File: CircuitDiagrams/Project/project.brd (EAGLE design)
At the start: 100 x 70 mm, 123 parts, among them IC1 UC3C, IC2 PCA9542A, IC3 MT48LC4M16A2TSOP54, IC4 TB6593FNGSSOP20, IC5 TB6593FNGSSOP20, J2 1BY2THROUGHHOLE, J3 1BY2THROUGHHOLE, J4 1BY2THROUGHHOLE, J5 8PIN1.27MM2X4TH, J6 4PIN1.27MM2X2TH, J7 1BY2THROUGHHOLE, J8 10PIN1.27MM2X5TH, Q1 OV7670, Q2 OV7670, Q3 VREGSOT-223, Q4 TCRT1010TH, Q5 TCRT1010TH, Q6 CSM-7X-DU, X2 MICROSDSMD

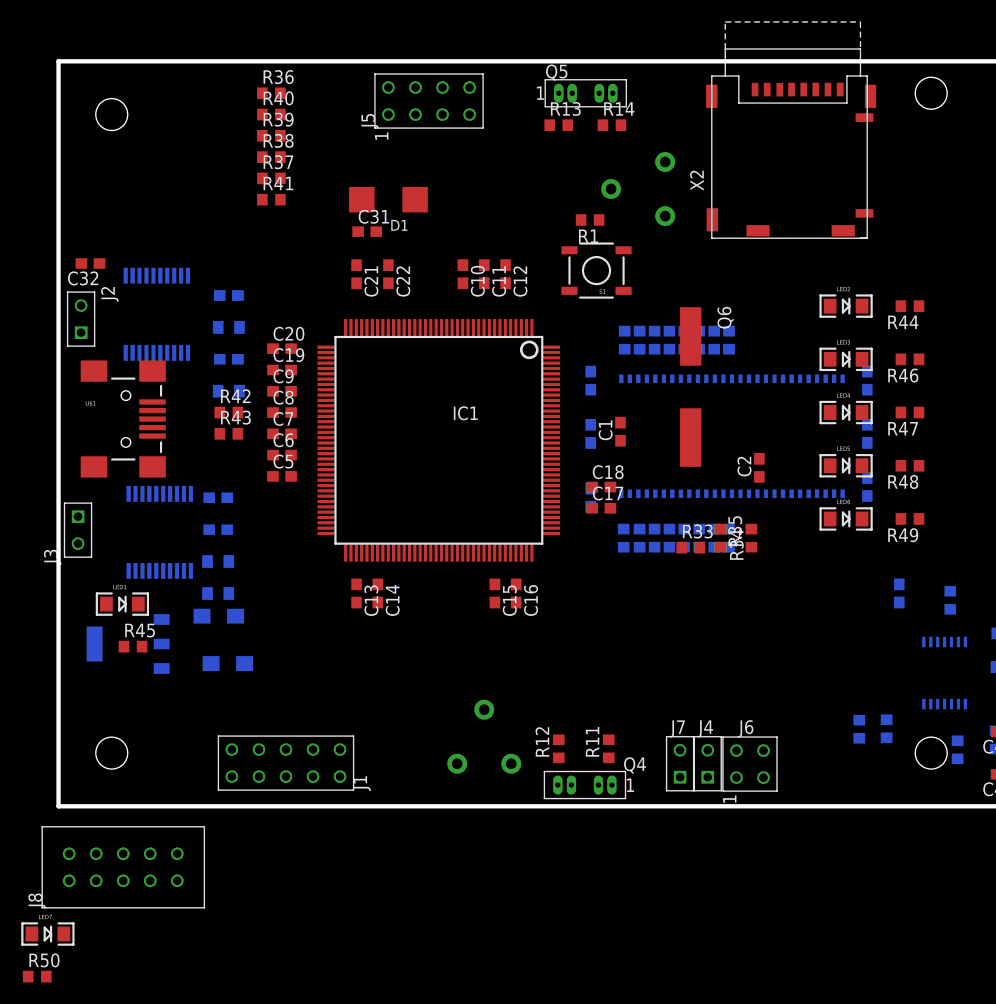
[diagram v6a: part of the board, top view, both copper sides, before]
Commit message: Changed the JTAG Package. Added Headers for all unused pins.
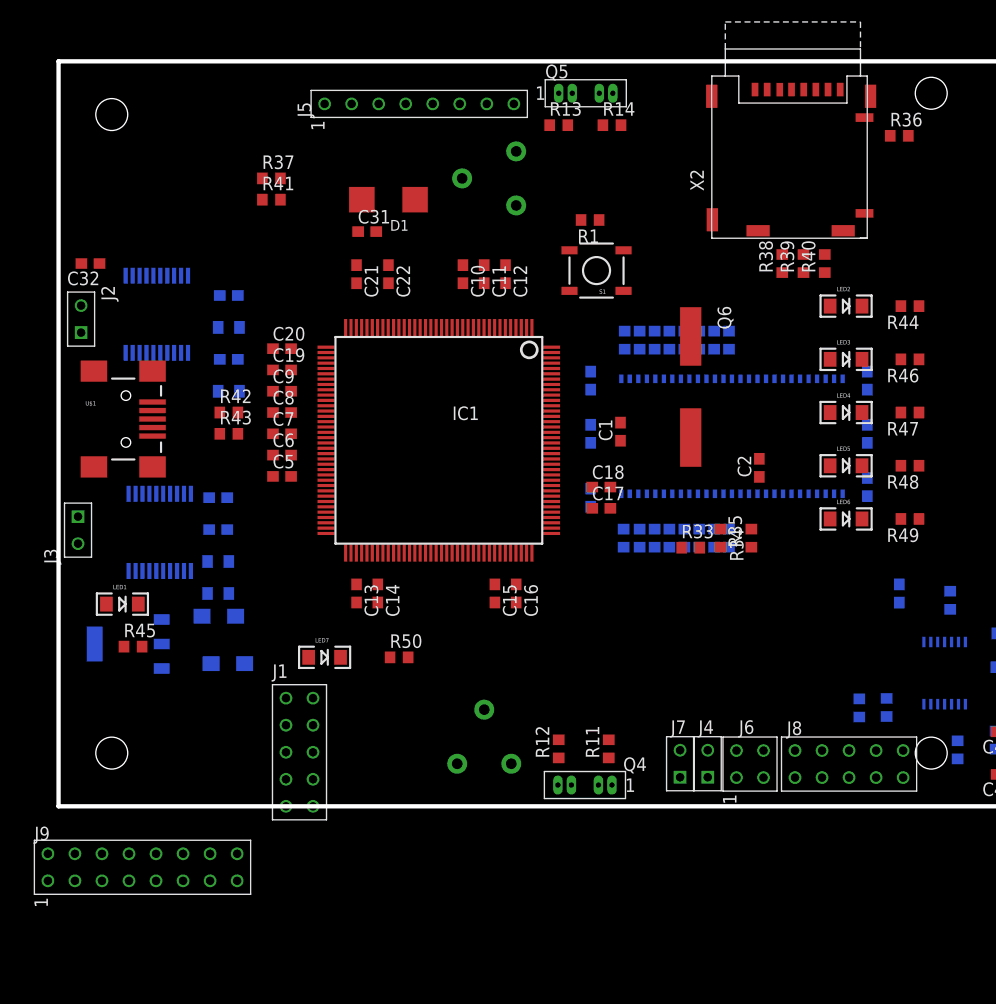
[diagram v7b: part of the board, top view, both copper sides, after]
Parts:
- added J9: 16PIN2.54MM2X8TH, Headers:2.54MM2X8TH
- J1: value (none) -> JTAG2.54MM2X5TH; device Headers:2BY5 -> Headers:2.54MM2X5TH
- J5: value 8PIN1.27MM2X4TH -> 8PIN2.54MM1X8TH; device Headers:1.27MM2X4TH -> Headers:2.54MM1X8TH
- J6: value 4PIN1.27MM2X2TH -> 4PIN2.54MM2X2TH; device Headers:1.27MM2X2TH -> Headers:2.54MM2X2TH
- J8: value 10PIN1.27MM2X5TH -> 10PIN2.54MM2X5TH; device Headers:1.27MM2X5TH -> Headers:2.54MM2X5TH
- moved J8 68.9 mm to (69.2, 2.70)
- moved R36 59.1 mm to (79.0, 63.0)
- moved R40 53.9 mm to (72.0, 51.0), turned to 90 degrees
- moved R39 51.4 mm to (70.0, 51.0), turned to 90 degrees
- moved R38 49.0 mm to (68.0, 51.0), turned to 90 degrees
- moved R50 45.3 mm to (32.0, 14.0)
- moved LED7 36.8 mm to (25.0, 14.0)
- moved R16 14.0 mm to (43.0, 59.0)
- moved J1 6.10 mm to (21.4, 10.2)
- moved J5 6.08 mm to (25.0, 66.0)
- moved R3 2.00 mm to (75.2, 9.24)
- moved R2 2.00 mm to (77.8, 9.29)
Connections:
- net PA10: now also J8.7; no longer J8.2
- net PA12: now also J8.8; no longer J8.3
- net PA13: now also J8.9; no longer J8.4
- net PA14: now also J8.10; no longer J8.5
- net PA5: now also J8.6; no longer J8.1
- net PC0: now also J9.16; no longer J8.10
- net PC1: now also J9.15; no longer J8.9
- net PC10: now also J9.11
- net PC11: now also J9.10
- net PC12: now also J9.9
- net PC13: now also J9.8; no longer J8.7
- net PC6: now also J9.14; no longer J8.8
- net PC7: now also J9.13
- net PC9: now also J9.12
- net PD16: now also J8.2
- net PD18: now also J8.3
- net PD19: now also J8.4
- net PD22: now also J8.5
- net PD23: now also J9.1
- net PD25: now also J9.2
- net PD26: now also J9.3
- net PD27: now also J9.4
- net PD28: now also J9.5
- net PD29: now also J9.6; no longer J8.6
- net PD30: now also J9.7
- net PD4: now also J8.1

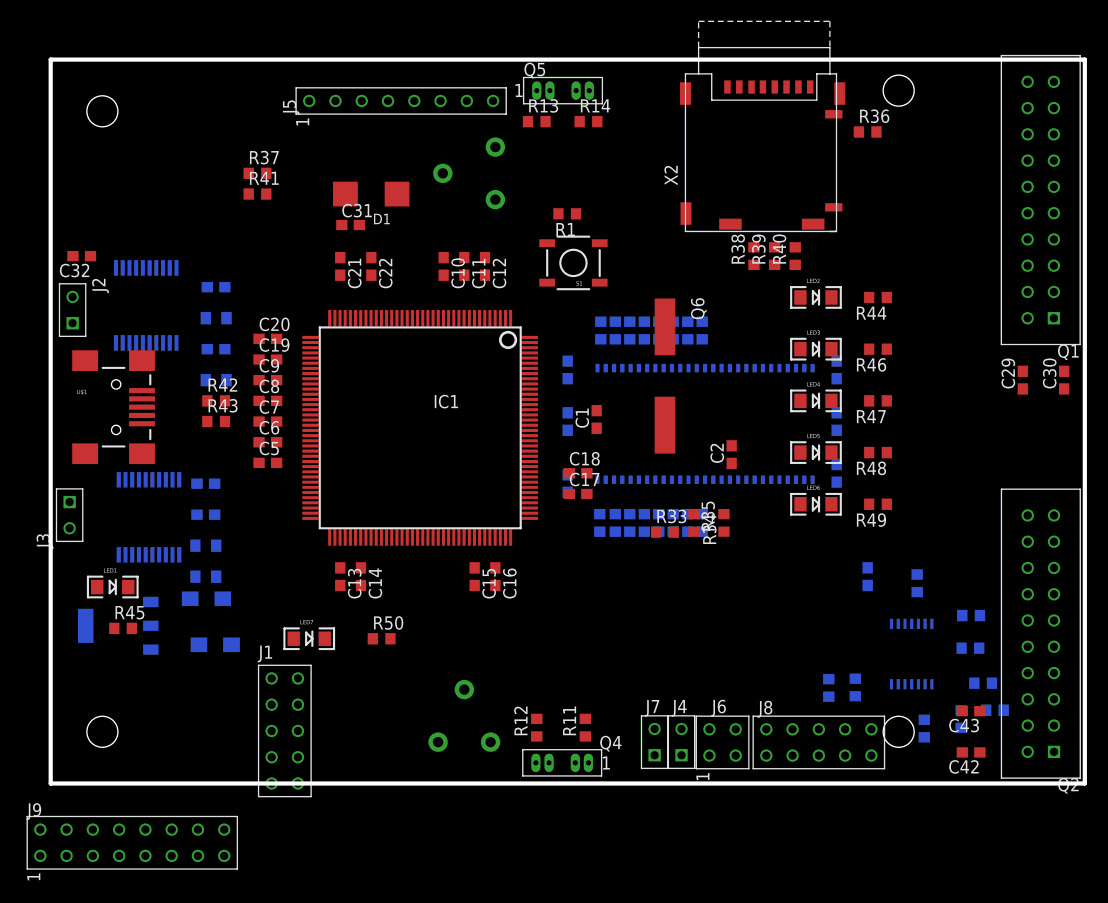
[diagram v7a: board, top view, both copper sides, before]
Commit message: Routed all +3V3 signals. Made into a four layer board.
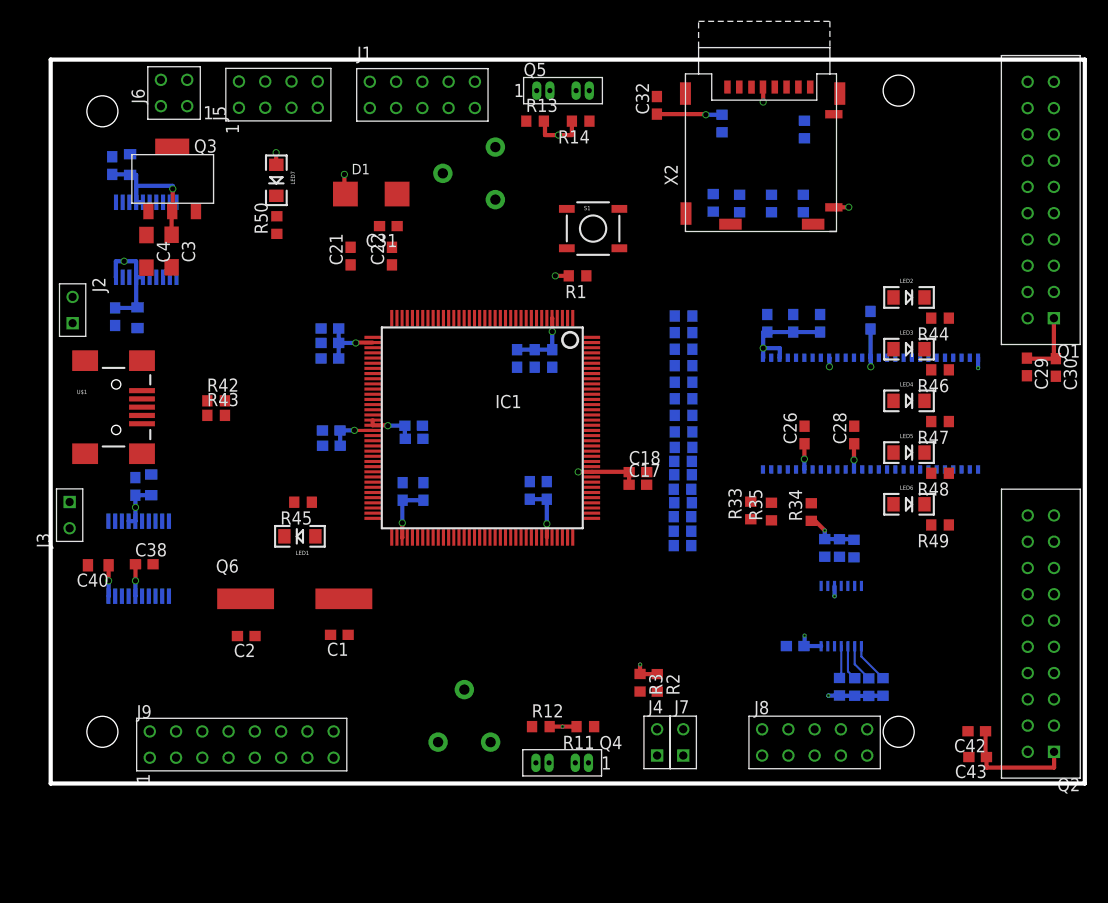
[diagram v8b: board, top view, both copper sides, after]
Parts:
- J5: value 8PIN2.54MM1X8TH -> 8PIN2.54MM2X4TH; device Headers:2.54MM1X8TH -> Headers:2.54MM2X4TH
- moved J6 80.6 mm to (13.2, 65.5), turned to 90 degrees
- moved C32 57.5 mm to (58.6, 65.6), turned to 90 degrees
- moved J1 56.0 mm to (30.9, 65.3), turned to 0 degrees
- moved C2 50.1 mm to (18.9, 14.3), turned to 180 degrees
- moved R41 45.4 mm to (64.9, 63.8), flipped to the bottom, turned to 270 degrees
- moved LED7 44.4 mm to (21.8, 58.3), turned to 270 degrees
- moved R37 44.2 mm to (64.1, 56.1), flipped to the bottom, turned to 90 degrees
- moved Q3 43.4 mm to (11.8, 58.3), flipped to the top, turned to 0 degrees
- moved Q6 41.8 mm to (23.6, 17.9), turned to 0 degrees
- moved R50 41.3 mm to (21.9, 54.0), turned to 90 degrees
- moved C3 38.3 mm to (11.7, 51.5), flipped to the top, turned to 270 degrees
- moved C4 34.1 mm to (9.26, 51.5), flipped to the top, turned to 270 degrees
- moved C1 32.4 mm to (27.9, 14.4), turned to 180 degrees
- moved C23 28.9 mm to (74.4, 44.5), turned to 90 degrees
- moved C24 22.3 mm to (71.8, 44.5), turned to 90 degrees
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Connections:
- net DM renamed USB_N
- net DP renamed USB_P
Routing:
- net +3V3: track 0.00 -> 154.4 mm, vias 0 -> 30
- net VDDCORE: track 0.00 -> 4.66 mm, vias 0 -> 1
- net INT1: track 0.00 -> 3.95 mm
- net SDA1: track 0.00 -> 3.67 mm
- net SCL1: track 0.00 -> 3.36 mm
- net INT: track 0.00 -> 3.14 mm
- added copper zone on layer 2, net +3V3
- added copper zone on layer 3, net GND
